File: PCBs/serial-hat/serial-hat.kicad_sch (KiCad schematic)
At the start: 17 parts, among them J1 CTS/RTS3, J2 TX/RX3, J3 CTS/RTS2, J4 TX/RX2, J5 UART3, J6 UART2, J7 Conn_02x20_Odd_Even, U1 MAX3232, U2 MAX3232

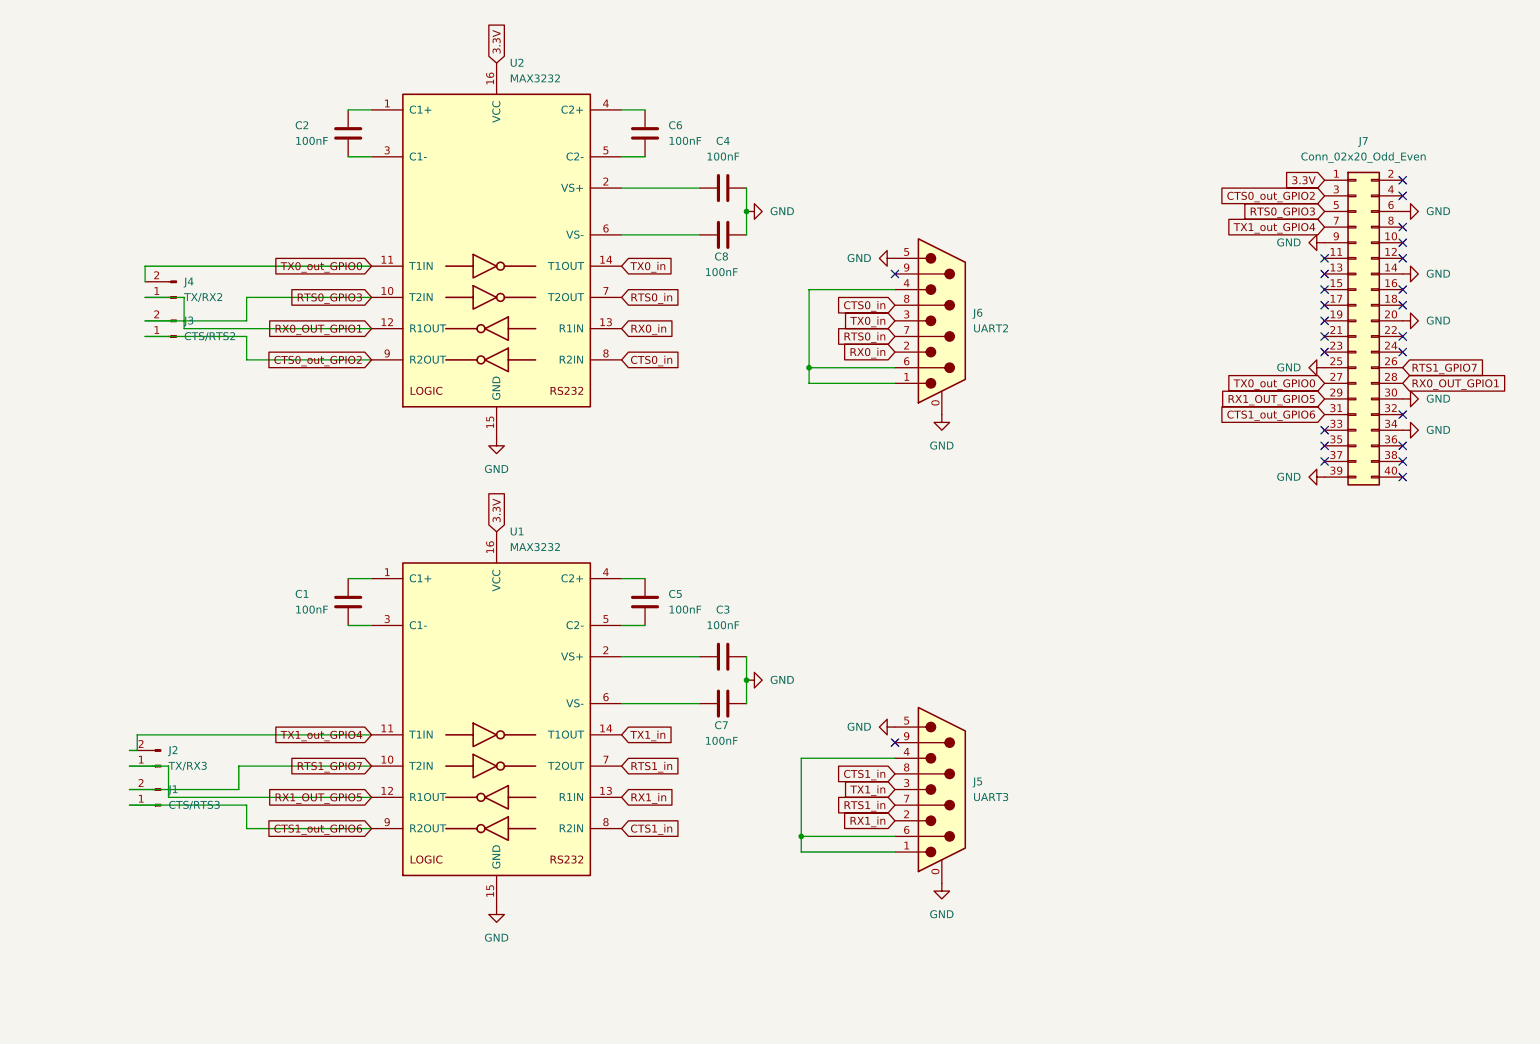
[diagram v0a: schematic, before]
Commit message: Rework for single MAX3232
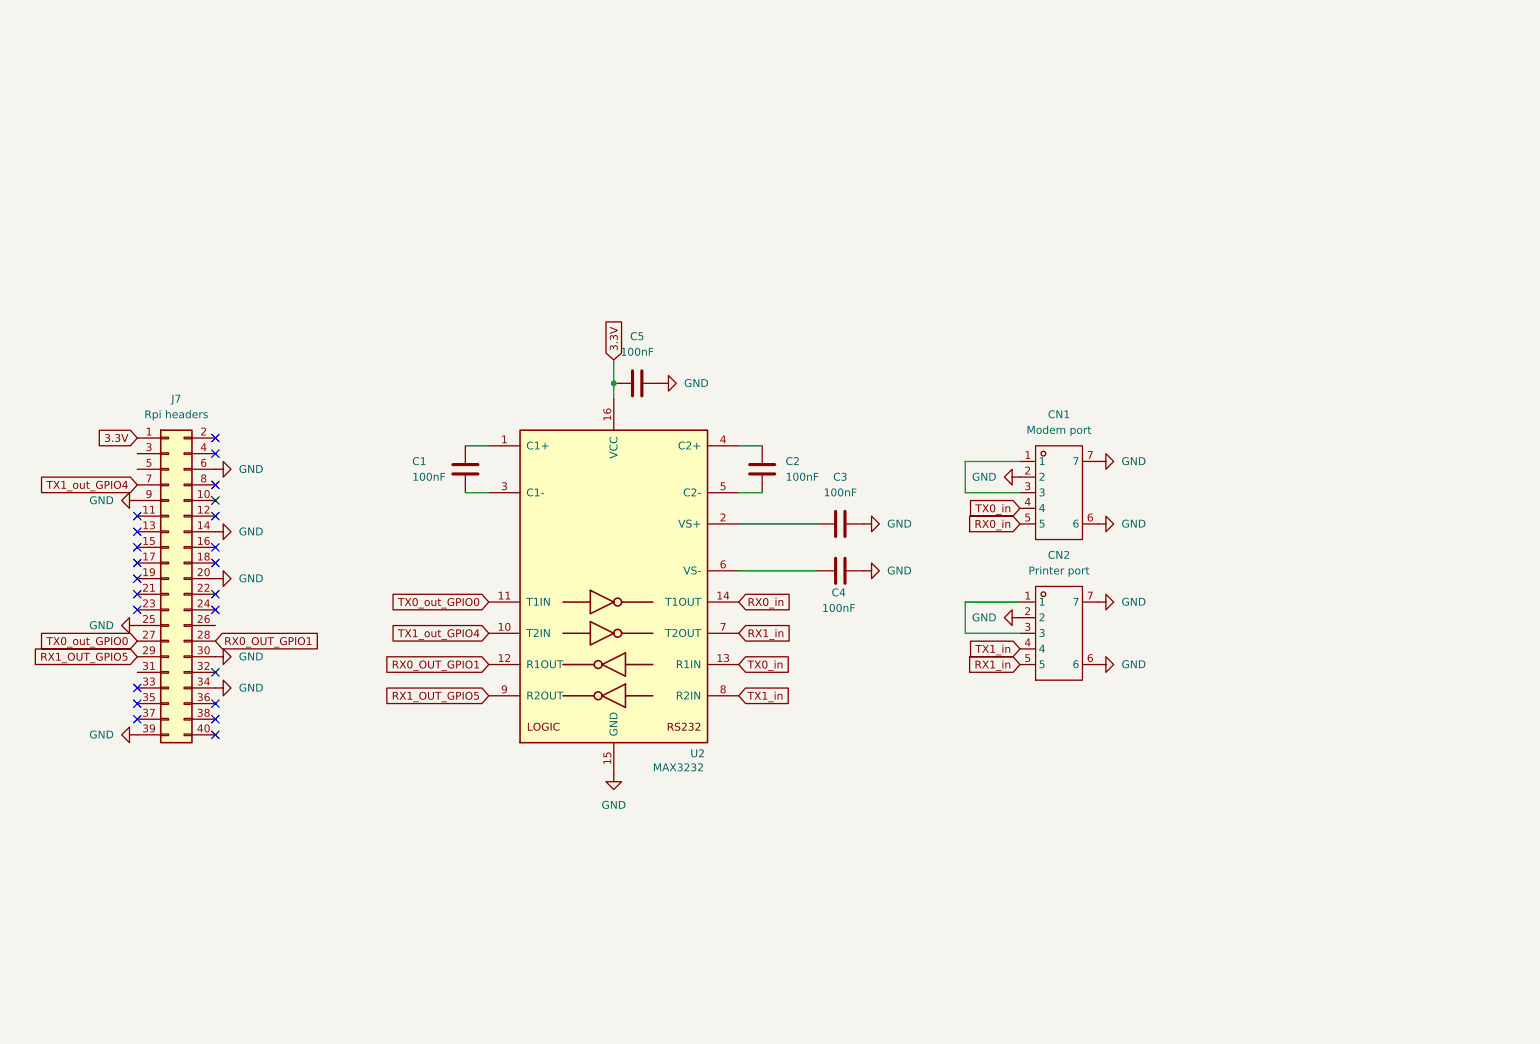
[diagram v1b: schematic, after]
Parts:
- removed C1, C3, C7: 100nF, Capacitor_THT:C_Disc_D5.0mm_W2.5mm_P2.50mm, symbol Device:C
- removed J1: CTS/RTS3, Connector_PinHeader_2.54mm:PinHeader_1x02_P2.54mm_Vertical, symbol Connector:Conn_01x02_Pin
- removed J2: TX/RX3, Connector_PinHeader_2.54mm:PinHeader_1x02_P2.54mm_Vertical, symbol Connector:Conn_01x02_Pin
- removed J3: CTS/RTS2, Connector_PinHeader_2.54mm:PinHeader_1x02_P2.54mm_Vertical, symbol Connector:Conn_01x02_Pin
- removed J4: TX/RX2, Connector_PinHeader_2.54mm:PinHeader_1x02_P2.54mm_Vertical, symbol Connector:Conn_01x02_Pin
- removed J5: UART3, Connector_Dsub:DSUB-9_Male_Horizontal_P2.77x2.84mm_EdgePinOffset7.70mm_Housed_MountingHolesOffset9.12mm, symbol Connector:DE9_Plug_MountingHoles
- removed J6: UART2, Connector_Dsub:DSUB-9_Male_Horizontal_P2.77x2.84mm_EdgePinOffset7.70mm_Housed_MountingHolesOffset9.12mm, symbol Connector:DE9_Plug_MountingHoles
- removed U1: MAX3232, Package_DIP:DIP-16_W7.62mm, symbol Interface_UART:MAX3232
- added CN1: Modem port, DIN5:CONN-TH_DIN-504-M10, symbol DIN:DIN-504
- added CN2: Printer port, DIN5:CONN-TH_DIN-504-M10, symbol DIN:DIN-504
- J7: value Conn_02x20_Odd_Even -> Rpi headers
- renumbered C2 to C1, C6 to C2, C4 to C3, C8 to C4
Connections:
- net CTS0_in is gone; now on net TX1_in: U2.8 (R2IN)
- net RTS0_in is gone; now on net RX1_in: U2.7 (T2OUT)
- net 3.3V: now also C5.1
- net GND: now also C5.2, CN1.2, CN1.6, CN1.7, CN2.2, CN2.6, CN2.7
- net RX0_in: now also U2.14 (T1OUT), CN1.5; no longer U2.13 (R1IN)
- net RX1_OUT_GPIO5: now also U2.9 (R2OUT)
- net RX1_in: now also CN2.5
- net TX0_in: now also U2.13 (R1IN), CN1.4; no longer U2.14 (T1OUT)
- net TX1_in: now also CN2.4
- net TX1_out_GPIO4: now also U2.10 (T2IN)
- net CTS0_out_GPIO2: no longer names the net of J7.3 (Pin_3)
- net CTS0_out_GPIO2: no longer U2.9 (R2OUT)
- net CTS1_out_GPIO6: no longer names the net of J7.31 (Pin_31)
- net RTS0_GPIO3: no longer names the net of J7.5 (Pin_5)
- net RTS0_GPIO3: no longer U2.10 (T2IN)
- net RTS1_GPIO7: no longer names the net of J7.26 (Pin_26)
- new net: CN2.1, CN2.3
- new net: CN1.1, CN1.3
- no-connect marks 25 -> 23
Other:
- moved on the sheet: C1, C2, C3, C4, J7, U2

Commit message: Test with Max232 + shifter
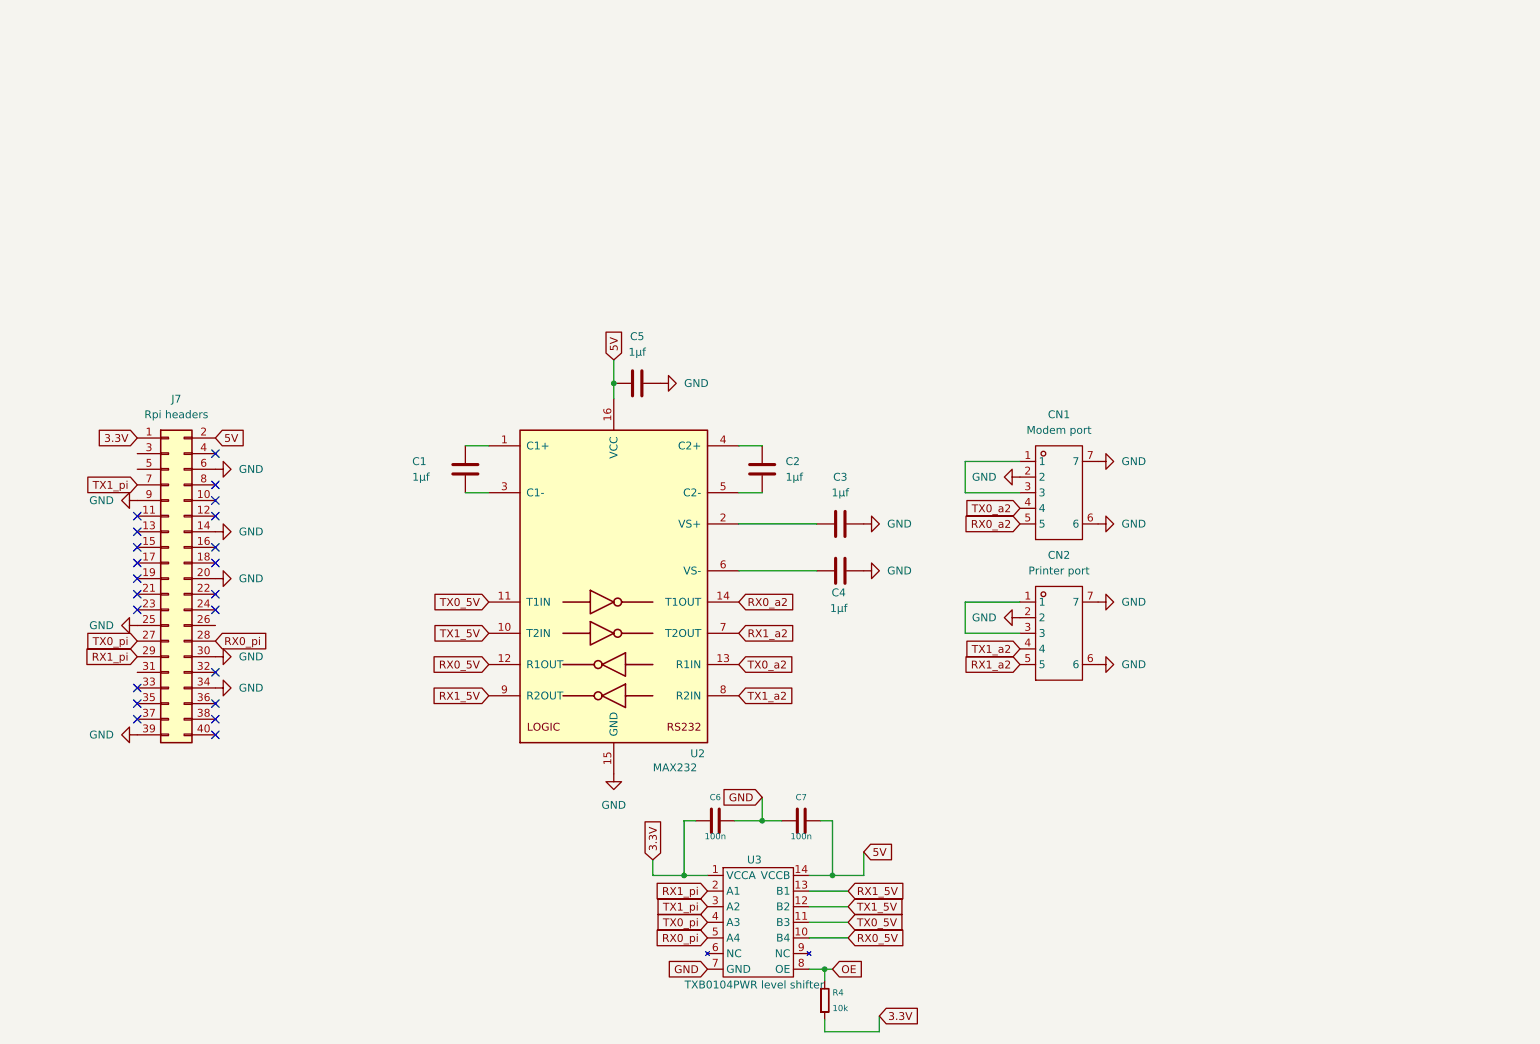
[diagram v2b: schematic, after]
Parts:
- added C6, C7: 100n, Capacitor_SMD:C_0603_1608Metric, symbol e-radionica.com schematics:0603C
- added R4: 10k, Resistor_SMD:R_0603_1608Metric, symbol e-radionica.com schematics:0603R
- added U3: TXB0104PWR level shifter, Package_SO:TSSOP-14-1EP_4.4x5mm_P0.65mm, symbol e-radionica.com schematics:TXB0104QPWRQ1
- C1, C2, C3, C4, C5: value 100nF -> 1µf; footprint Capacitor_THT:C_Disc_D5.0mm_W2.5mm_P2.50mm -> Capacitor_SMD:C_0603_1608Metric; LCSC C353903 -> C15849
- U2: value MAX3232 -> MAX232; footprint Package_DIP:DIP-16_W7.62mm -> Package_SO:SOIC-16_3.9x9.9mm_P1.27mm; LCSC C7432161 -> C59824
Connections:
- net 3.3V: now also C6.1, R4.1, U3.1 (VCCA); no longer C5.1, U2.16 (VCC)
- net GND: now also C6.2, C7.1, U3.7 (GND)
- net 5V: now reaches J7.2 (Pin_2)
- net 5V: now also C5.1, U2.16 (VCC), C7.2, U3.14 (VCCB)
- net RX0_OUT_GPIO1 renamed RX0_5V
- net RX0_5V: now also U3.10 (B4); no longer J7.28 (Pin_28)
- net RX0_in renamed RX0_a2
- net RX1_OUT_GPIO5 renamed RX1_5V
- net RX1_5V: now also U3.13 (B1); no longer J7.29 (Pin_29)
- net RX1_in renamed RX1_a2
- net TX0_in renamed TX0_a2
- net TX0_out_GPIO0 renamed TX0_5V
- net TX0_5V: now also U3.11 (B3); no longer J7.27 (Pin_27)
- net TX1_in renamed TX1_a2
- net TX1_out_GPIO4 renamed TX1_5V
- net TX1_5V: now also U3.12 (B2); no longer J7.7 (Pin_7)
- new net OE: R4.2, U3.8 (OE)
- new net RX0_pi: J7.28 (Pin_28), U3.5 (A4)
- new net RX1_pi: J7.29 (Pin_29), U3.2 (A1)
- new net TX0_pi: J7.27 (Pin_27), U3.4 (A3)
- new net TX1_pi: J7.7 (Pin_7), U3.3 (A2)
- no-connect marks 23 -> 22

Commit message: Back to MAX3232
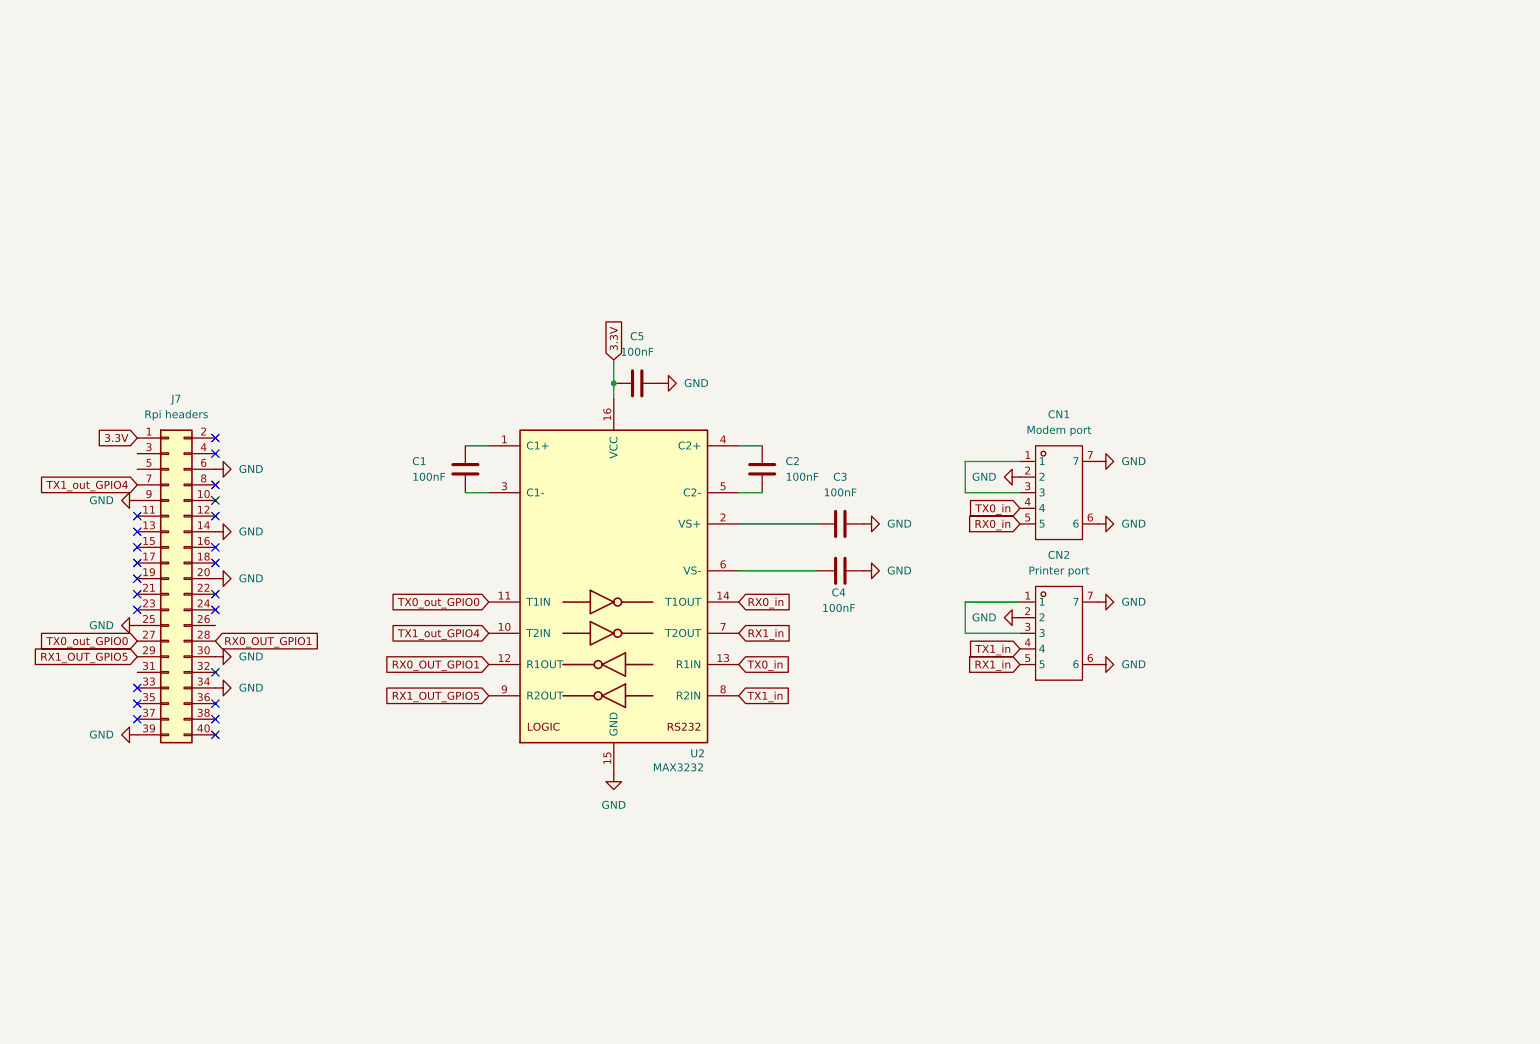
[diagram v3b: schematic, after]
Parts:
- removed C6, C7: 100n, Capacitor_SMD:C_0603_1608Metric, symbol e-radionica.com schematics:0603C
- removed R4: 10k, Resistor_SMD:R_0603_1608Metric, symbol e-radionica.com schematics:0603R
- removed U3: TXB0104PWR level shifter, Package_SO:TSSOP-14-1EP_4.4x5mm_P0.65mm, symbol e-radionica.com schematics:TXB0104QPWRQ1
- C1, C2, C3, C4, C5: value 1µf -> 100nF; LCSC C15849 -> C14663
- U2: value MAX232 -> MAX3232; LCSC C59824 -> C193666
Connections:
- net RX0_pi is gone; now on net RX0_OUT_GPIO1: J7.28 (Pin_28)
- net RX1_pi is gone; now on net RX1_OUT_GPIO5: J7.29 (Pin_29)
- net TX0_pi is gone; now on net TX0_out_GPIO0: J7.27 (Pin_27)
- net TX1_pi is gone; now on net TX1_out_GPIO4: J7.7 (Pin_7)
- net 3.3V: now also C5.1, U2.16 (VCC)
- removed net 5V: C5.1, J7.2 (Pin_2), U2.16 (VCC)
- net RX0_5V renamed RX0_OUT_GPIO1
- net RX0_a2 renamed RX0_in
- net RX1_5V renamed RX1_OUT_GPIO5
- net RX1_a2 renamed RX1_in
- net TX0_5V renamed TX0_out_GPIO0
- net TX0_a2 renamed TX0_in
- net TX1_5V renamed TX1_out_GPIO4
- net TX1_a2 renamed TX1_in
- no-connect marks 22 -> 23

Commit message: WIP - CISD
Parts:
- added R1, R2: 3.3k, Resistor_SMD:R_0603_1608Metric, symbol Device:R_US
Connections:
- net TX0_in: now also R1.2; no longer U2.13 (R1IN)
- net TX1_in: now also R2.2; no longer U2.8 (R2IN)
- new net: R1.1, U2.13 (R1IN)
- new net: R2.1, U2.8 (R2IN)
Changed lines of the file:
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@@
 	(global_label "TX0_in"
 		(shape input)
-		(at 135.89 128.27 0)
+		(at 143.51 128.27 0)
 		(fields_autoplaced yes)
 		(effects
@@
 		)
 		(property "Intersheetrefs" "${INTERSHEET_REFS}"
-			(at 144.9832 128.27 0)
+			(at 152.6032 128.27 0)
 			(effects
 				(font
@@
 	(global_label "TX1_in"
 		(shape input)
-		(at 135.89 133.35 0)
+		(at 143.51 133.35 0)
 		(fields_autoplaced yes)
 		(effects
@@
 		)
 		(property "Intersheetrefs" "${INTERSHEET_REFS}"
-			(at 144.9832 133.35 0)
+			(at 152.6032 133.35 0)
 			(effects
 				(font
@@
 				(justify left)
 				(hide yes)
+			)
+		)
+	)
+	(symbol
+		(lib_id "Device:R_US")
+		(at 139.7 128.27 90)
+		(unit 1)
+		(exclude_from_sim no)
+		(in_bom yes)
+		(on_board yes)
+		(dnp no)
+		(property "Reference" "R1"
+			(at 137.922 126.238 90)
+			(effects
+				(font
+					(size 1.27 1.27)
+				)
+			)
+		)
+		(property "Value" "3.3k"
+			(at 142.748 126.238 90)
+			(effects
+				(font
+					(size 1.27 1.27)
+				)
+			)
+		)
+		(property "Footprint" "Resistor_SMD:R_0603_1608Metric"
+			(at 139.954 127.254 90)
+			(effects
+				(font
+					(size 1.27 1.27)
+				)
+				(hide yes)
+			)
+		)
+		(property "Datasheet" "~"
+			(at 139.7 128.27 0)
+			(effects
+				(font
+					(size 1.27 1.27)
+				)
+				(hide yes)
+			)
+		)
+		(property "Description" "Resistor, US symbol"
+			(at 139.7 128.27 0)
+			(effects
+				(font
+					(size 1.27 1.27)
+				)
+				(hide yes)
+			)
+		)
+		(property "LCSC" "C21190"
+			(at 139.7 128.27 90)
+			(effects
+				(font
+					(size 1.27 1.27)
+				)
+				(hide yes)
+			)
+		)
+		(pin "2"
+		)
+		(pin "1"
+		)
+		(instances
+			(project "serial-hat"
+				(path "/f30a5902-bf77-48c6-ab50-b8e2235ec207"
+					(reference "R1")
+					(unit 1)
+				)
 			)
 		)
@@
 					(unit 1)
 				)
+			)
+		)
+	)
+	(symbol
+		(lib_id "Device:R_US")
+		(at 139.7 133.35 90)
+		(unit 1)
+		(exclude_from_sim no)
+		(in_bom yes)
+		(on_board yes)
+		(dnp no)
+		(property "Reference" "R2"
+			(at 137.922 131.318 90)
+			(effects
+				(font
+					(size 1.27 1.27)
+				)
+			)
+		)
+		(property "Value" "3.3k"
+			(at 142.748 131.318 90)
+			(effects
+				(font
+					(size 1.27 1.27)
+				)
+			)
+		)
+		(property "Footprint" "Resistor_SMD:R_0603_1608Metric"
+			(at 139.954 132.334 90)
+			(effects
+				(font
+					(size 1.27 1.27)
+				)
+				(hide yes)
+			)
+		)
+		(property "Datasheet" "~"
+			(at 139.7 133.35 0)
+			(effects
+				(font
+					(size 1.27 1.27)
+				)
+				(hide yes)
+			)
+		)
+		(property "Description" "Resistor, US symbol"
+			(at 139.7 133.35 0)
+			(effects
+				(font
+					(size 1.27 1.27)
+				)
+				(hide yes)
+			)
+		)
+		(property "LCSC" "C21190"
+			(at 139.7 133.35 90)
+			(effects
+				(font
+					(size 1.27 1.27)
+				)
+				(hide yes)
+			)
+		)
+		(pin "2"
+		)
+		(pin "1"
+		)
+		(instances
+			(project "serial-hat"
+				(path "/f30a5902-bf77-48c6-ab50-b8e2235ec207"
+					(reference "R2")
+					(unit 1)
+				)
